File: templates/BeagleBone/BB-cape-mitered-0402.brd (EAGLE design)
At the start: 86.4 x 54.6 mm, 14 parts, among them IC8 EEPROM-I2CSMD

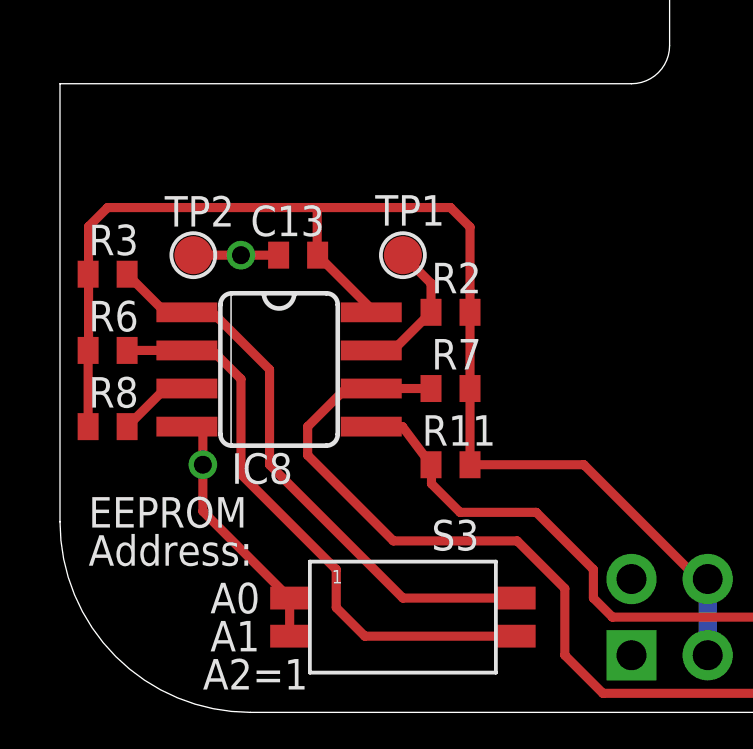
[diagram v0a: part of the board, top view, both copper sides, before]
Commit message: renumbered components on templates
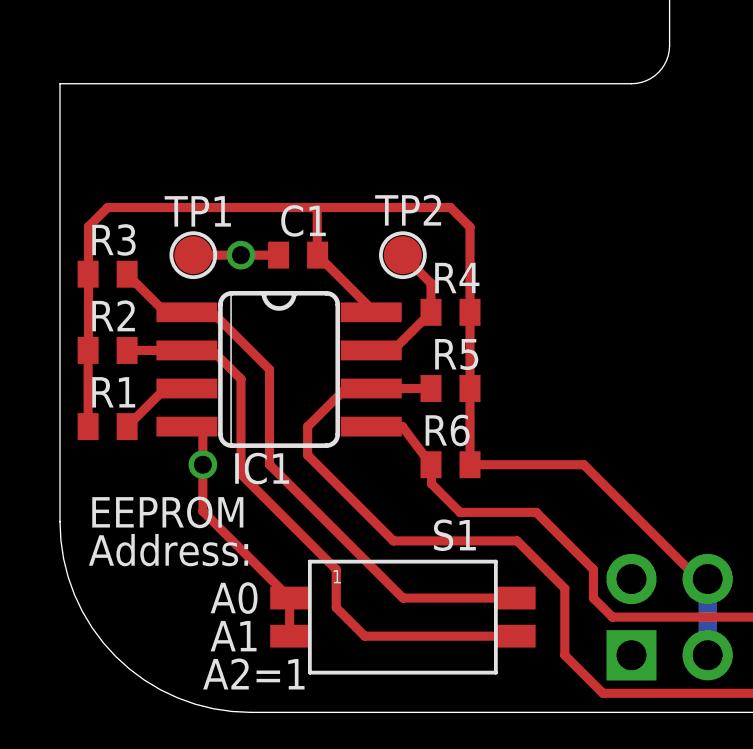
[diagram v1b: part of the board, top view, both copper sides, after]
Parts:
- removed R11: 5.6k, logic-supply:R0402
- added R4: 5.6k, logic-supply:R0402
- moved R6 12.0 mm to (13.0, 8.26), turned to 0 degrees
- moved R2 11.5 mm to (1.59, 12.1), turned to 180 degrees
- moved TP1 6.98 mm to (4.45, 15.2)
- moved TP2 6.98 mm to (11.4, 15.2)
- renumbered C13 to C1, IC8 to IC1, R7 to R5, R8 to R1, S3 to S1
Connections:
- net 3.3V: now also R4.2; no longer R11.2
- net GND: now also TP1.P$1; no longer TP2.P$1
- net I2C2_SDA: now also R6.1; no longer R11.1
- net N$14: now also R2.1; no longer R6.1
- net WP: now also R4.1, TP2.P$1; no longer R2.1, TP1.P$1
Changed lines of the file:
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@@
 </autorouter>
 <elements>
-<element name="IC8" library="logic-supply" package="SO08" value="EEPROM-I2CSMD" x="7.3025" y="11.43" smashed="yes" rot="R270">
+<element name="IC1" library="logic-supply" package="SO08" value="EEPROM-I2CSMD" x="7.3025" y="11.43" smashed="yes" rot="R270">
 <attribute name="VALUE" x="6.6675" y="12.7" size="0.4064" layer="27" rot="R270"/>
 <attribute name="NAME" x="5.715" y="7.62" size="1.016" layer="25" font="vector"/>
@@
 </element>
 <element name="U$4" library="logic-supply" package="LOGO-LGX-LARGE" value="LOGO-LGX_LARGE" x="41.5925" y="31.75" smashed="yes"/>
-<element name="R7" library="logic-supply" package="R0402" value="5.6k" x="13.0175" y="10.795" smashed="yes">
+<element name="R5" library="logic-supply" package="R0402" value="5.6k" x="13.0175" y="10.795" smashed="yes">
 <attribute name="NAME" x="12.3825" y="11.43" size="1.016" layer="25" font="vector"/>
 <attribute name="VALUE" x="12.3825" y="8.89" size="1.27" layer="27"/>
 <attribute name="PARTNO" value="RC0603FR-074K7L" x="13.0175" y="10.795" size="1.778" layer="27" display="off"/>
 </element>
-<element name="R11" library="logic-supply" package="R0402" value="5.6k" x="13.0175" y="8.255" smashed="yes">
+<element name="R6" library="logic-supply" package="R0402" value="5.6k" x="13.0175" y="8.255" smashed="yes">
 <attribute name="NAME" x="12.065" y="8.89" size="1.016" layer="25" font="vector"/>
 <attribute name="VALUE" x="12.3825" y="6.35" size="1.27" layer="27"/>
 <attribute name="PARTNO" value="RC0603FR-074K7L" x="13.0175" y="8.255" size="1.778" layer="27" display="off"/>
 </element>
-<element name="R2" library="logic-supply" package="R0402" value="5.6k" x="13.0175" y="13.335" smashed="yes">
+<element name="R4" library="logic-supply" package="R0402" value="5.6k" x="13.0175" y="13.335" smashed="yes">
 <attribute name="NAME" x="12.3825" y="13.97" size="1.016" layer="25" font="vector"/>
 <attribute name="VALUE" x="12.3825" y="11.43" size="1.27" layer="27"/>
 <attribute name="PARTNO" value="RC0603FR-074K7L" x="13.0175" y="13.335" size="1.778" layer="27" display="off"/>
 </element>
-<element name="TP1" library="logic-supply" package="TEST_POINT" value="TEST_POINT" x="11.43" y="15.24" smashed="yes">
+<element name="TP2" library="logic-supply" package="TEST_POINT" value="TEST_POINT" x="11.43" y="15.24" smashed="yes">
 <attribute name="NAME" x="10.50925" y="16.22425" size="1.016" layer="25" font="vector"/>
 <attribute name="VALUE" x="12.573" y="14.605" size="0.4064" layer="27" ratio="10"/>
@@
 <attribute name="PARTNO" value="RC0603FR-074K7L" x="1.5875" y="14.605" size="1.778" layer="27" rot="R180" display="off"/>
 </element>
-<element name="R6" library="logic-supply" package="R0402" value="5.6k" x="1.5875" y="12.065" smashed="yes" rot="R180">
+<element name="R2" library="logic-supply" package="R0402" value="5.6k" x="1.5875" y="12.065" smashed="yes" rot="R180">
 <attribute name="NAME" x="0.9525" y="12.7" size="1.016" layer="25" font="vector"/>
 <attribute name="VALUE" x="2.2225" y="13.97" size="1.27" layer="27" rot="R180"/>
 <attribute name="PARTNO" value="RC0603FR-074K7L" x="1.5875" y="12.065" size="1.778" layer="27" rot="R180" display="off"/>
 </element>
-<element name="R8" library="logic-supply" package="R0402" value="5.6k" x="1.5875" y="9.525" smashed="yes" rot="R180">
+<element name="R1" library="logic-supply" package="R0402" value="5.6k" x="1.5875" y="9.525" smashed="yes" rot="R180">
 <attribute name="NAME" x="0.9525" y="10.16" size="1.016" layer="25" font="vector"/>
 <attribute name="VALUE" x="2.2225" y="11.43" size="1.27" layer="27" rot="R180"/>
 <attribute name="PARTNO" value="RC0603FR-074K7L" x="1.5875" y="9.525" size="1.778" layer="27" rot="R180" display="off"/>
 </element>
-<element name="C13" library="logic-supply" package="C0402" value="0.1uF" x="7.9375" y="15.24" smashed="yes" rot="R180">
-<attribute name="NAME" x="6.35" y="15.875" size="1.016" layer="25" font="vector"/>
+<element name="C1" library="logic-supply" package="C0402" value="0.1uF" x="7.9375" y="15.24" smashed="yes" rot="R180">
+<attribute name="NAME" x="7.3025" y="15.875" size="1.016" layer="25" font="vector"/>
 <attribute name="VALUE" x="8.5725" y="17.145" size="1.27" layer="27" rot="R180"/>
 <attribute name="PARTNO" value="C1608X7R1E104K080AA" x="7.9375" y="15.24" size="1.778" layer="27" rot="R180" display="off"/>
 </element>
-<element name="S3" library="logic-supply" package="DIPSWITCH-2P-SMD-1.27" value="SW_DIP-2P" x="11.43" y="3.175" smashed="yes">
+<element name="S1" library="logic-supply" package="DIPSWITCH-2P-SMD-1.27" value="SW_DIP-2P" x="11.43" y="3.175" smashed="yes">
 <attribute name="NAME" x="12.3825" y="5.3975" size="1.016" layer="25" font="vector"/>
 <attribute name="VALUE" x="8.89" y="-0.635" size="1.27" layer="27"/>
@@
 <element name="BB1" library="logic-supply" package="BB_CAPE_TOP" value="BBH2" x="0" y="0" rot="MR90"/>
 <element name="U$7" library="logic-supply" package="OSHW-LOGO-M" value="OSHW-LOGOM" x="63.8175" y="31.75"/>
-<element name="TP2" library="logic-supply" package="TEST_POINT" value="TEST_POINT" x="4.445" y="15.24" smashed="yes">
+<element name="TP1" library="logic-supply" package="TEST_POINT" value="TEST_POINT" x="4.445" y="15.24" smashed="yes">
 <attribute name="BOM" value="EXCLUDE" x="4.445" y="15.24" size="1.778" layer="27" display="off"/>
 <attribute name="DATABASE" value="./../BOM/logic-supply-db.txt" x="4.445" y="15.24" size="1.778" layer="27" display="off"/>
@@
 <signals>
 <signal name="3.3V">
-<contactref element="R7" pad="2"/>
-<contactref element="R11" pad="2"/>
+<contactref element="R5" pad="2"/>
+<contactref element="R6" pad="2"/>
+<contactref element="R4" pad="2"/>
+<contactref element="IC1" pad="8"/>
+<contactref element="R3" pad="2"/>
 <contactref element="R2" pad="2"/>
-<contactref element="IC8" pad="8"/>
-<contactref element="R3" pad="2"/>
-<contactref element="R6" pad="2"/>
-<contactref element="R8" pad="2"/>
-<contactref element="C13" pad="1"/>
+<contactref element="R1" pad="2"/>
+<contactref element="C1" pad="1"/>
 <contactref element="BB1" pad="P9.3"/>
 <contactref element="BB1" pad="P9.4"/>
@@
 </signal>
 <signal name="GND">
-<contactref element="C13" pad="2"/>
-<contactref element="S3" pad="1A"/>
-<contactref element="S3" pad="2A"/>
-<contactref element="IC8" pad="4"/>
+<contactref element="C1" pad="2"/>
+<contactref element="S1" pad="1A"/>
+<contactref element="S1" pad="2A"/>
+<contactref element="IC1" pad="4"/>
 <wire x1="7.655" y1="2.54" x2="7.655" y2="3.81" width="0.3048" layer="1"/>
 <via x="4.7625" y="8.255" extent="1-16" drill="0.6"/>
@@
 <contactref element="BB1" pad="P9.44"/>
 <contactref element="BB1" pad="P9.46"/>
-<contactref element="TP2" pad="P$1"/>
+<contactref element="TP1" pad="P$1"/>
 <wire x1="6.0325" y1="15.24" x2="4.445" y2="15.24" width="0.3048" layer="1"/>
 <wire x1="4.7625" y1="15.24" x2="4.445" y2="15.24" width="0" layer="19" extent="1-16"/>
@@
 </signal>
 <signal name="I2C2_SDA">
-<contactref element="IC8" pad="5"/>
-<contactref element="R11" pad="1"/>
+<contactref element="IC1" pad="5"/>
+<contactref element="R6" pad="1"/>
 <wire x1="41.91" y1="4.1275" x2="40.9575" y2="3.175" width="0.3048" layer="1"/>
 <wire x1="40.9575" y1="3.175" x2="18.415" y2="3.175" width="0.3048" layer="1"/>
@@
 </signal>
 <signal name="I2C2_SCL">
-<contactref element="IC8" pad="6"/>
-<contactref element="R7" pad="1"/>
+<contactref element="IC1" pad="6"/>
+<contactref element="R5" pad="1"/>
 <wire x1="41.91" y1="1.5875" x2="40.9575" y2="0.635" width="0.3048" layer="1"/>
 <wire x1="40.9575" y1="0.635" x2="18.0975" y2="0.635" width="0.3048" layer="1"/>
@@
 </signal>
 <signal name="WP">
-<contactref element="IC8" pad="7"/>
-<contactref element="TP1" pad="P$1"/>
-<contactref element="R2" pad="1"/>
+<contactref element="IC1" pad="7"/>
+<contactref element="TP2" pad="P$1"/>
+<contactref element="R4" pad="1"/>
 <wire x1="10.3759" y1="12.065" x2="11.0975" y2="12.065" width="0.3048" layer="1"/>
 <wire x1="11.0975" y1="12.065" x2="12.3675" y2="13.335" width="0.3048" layer="1"/>
@@
 </signal>
 <signal name="N$13">
-<contactref element="IC8" pad="1"/>
+<contactref element="IC1" pad="1"/>
 <contactref element="R3" pad="1"/>
-<contactref element="S3" pad="1B"/>
+<contactref element="S1" pad="1B"/>
 <wire x1="15.205" y1="3.81" x2="11.43" y2="3.81" width="0.3048" layer="1"/>
 <wire x1="4.2291" y1="13.335" x2="3.5075" y2="13.335" width="0.3048" layer="1"/>
@@
 </signal>
 <signal name="N$14">
-<contactref element="IC8" pad="2"/>
-<contactref element="R6" pad="1"/>
-<contactref element="S3" pad="2B"/>
+<contactref element="IC1" pad="2"/>
+<contactref element="R2" pad="1"/>
+<contactref element="S1" pad="2B"/>
 <wire x1="15.205" y1="2.54" x2="10.16" y2="2.54" width="0.3048" layer="1"/>
 <wire x1="10.16" y1="2.54" x2="9.2075" y2="3.4925" width="0.3048" layer="1"/>
@@
 </signal>
 <signal name="N$15">
-<contactref element="IC8" pad="3"/>
-<contactref element="R8" pad="1"/>
+<contactref element="IC1" pad="3"/>
+<contactref element="R1" pad="1"/>
 <wire x1="4.2291" y1="10.795" x2="3.5075" y2="10.795" width="0.3048" layer="1"/>
 <wire x1="3.5075" y1="10.795" x2="2.2375" y2="9.525" width="0.3048" layer="1"/>
